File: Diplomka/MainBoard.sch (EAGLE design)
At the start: 2 parts, among them U1 ESP32-WROOM-32

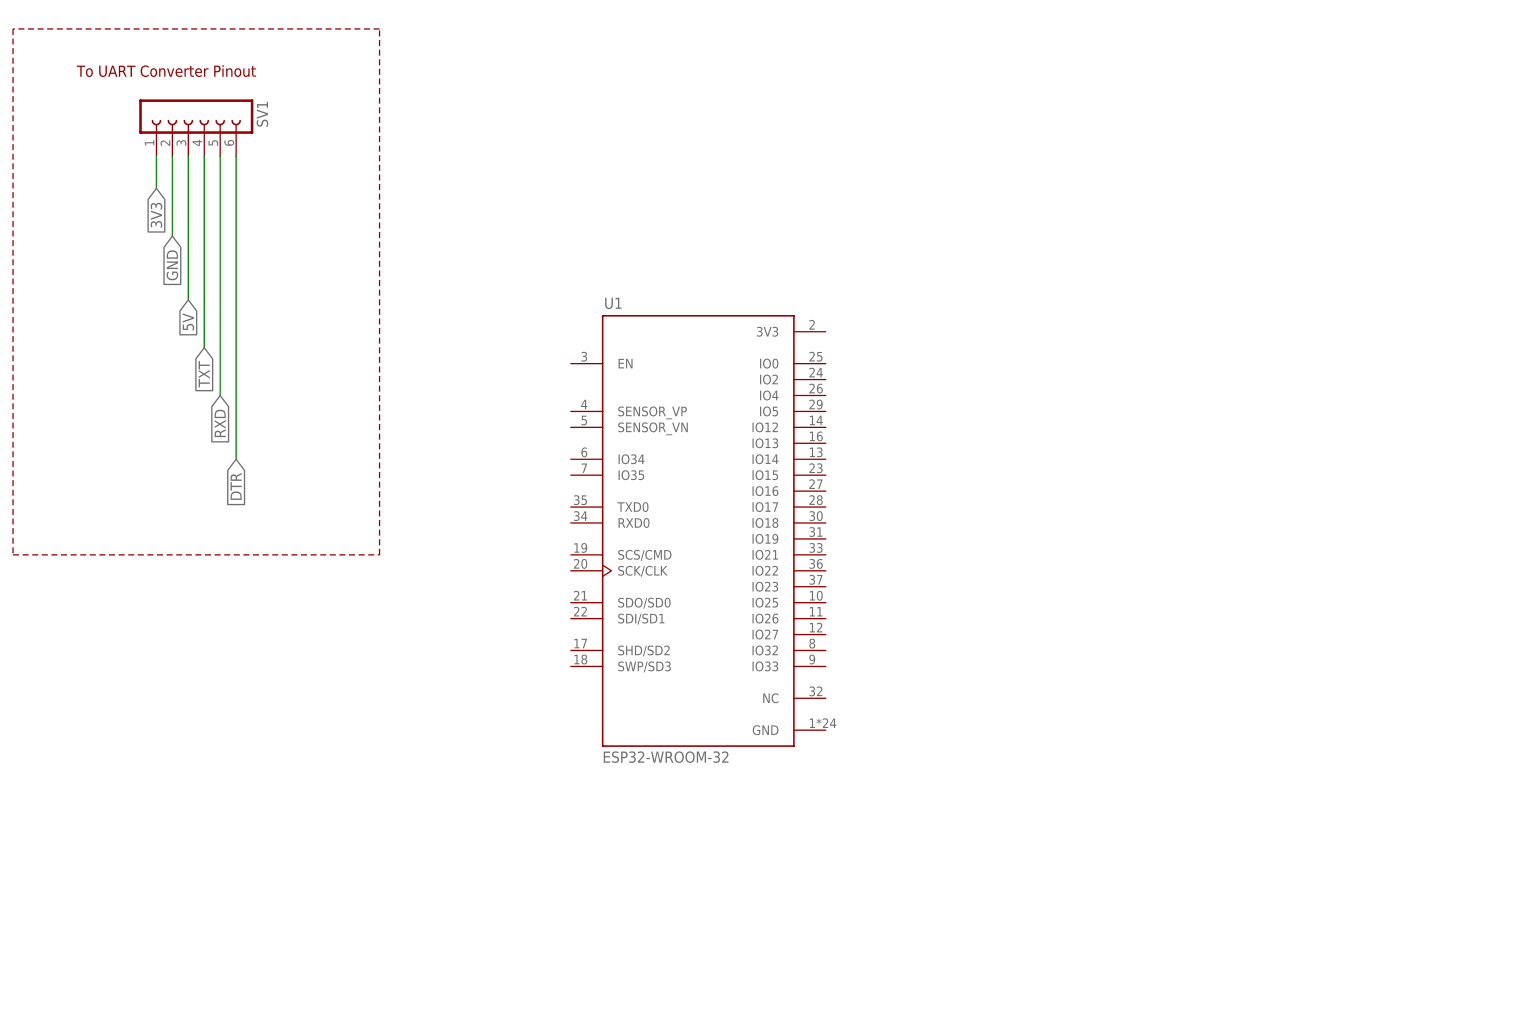
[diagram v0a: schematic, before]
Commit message: Added battery switch IC to schematic and library. 	# Please enter the commit message for your changes. Lines starting 	# with '#' will be ignored, and an empty message aborts the commit. 	# 	# On branch main 	# Your branch is up to date with 'origin/main'. 	# 	# Changes to be committed: 	#	modified:   MainBoard.brd 	#	modified:   MainBoard.s#1 	#	modified:   MainBoard.s#2 	#	modified:   MainBoard.s#3 	#	modified:   MainBoard.s#4 	#	modified:   MainBoard.sch 	#	modified:   eagle.epf 	# 	# Untracked files: 	#	Eagle_WR-USB (rev22c).lbr 	#	MainBoard.b#1 	#	MainBoard.s#5 	#	texas-instruments.lbr 	#
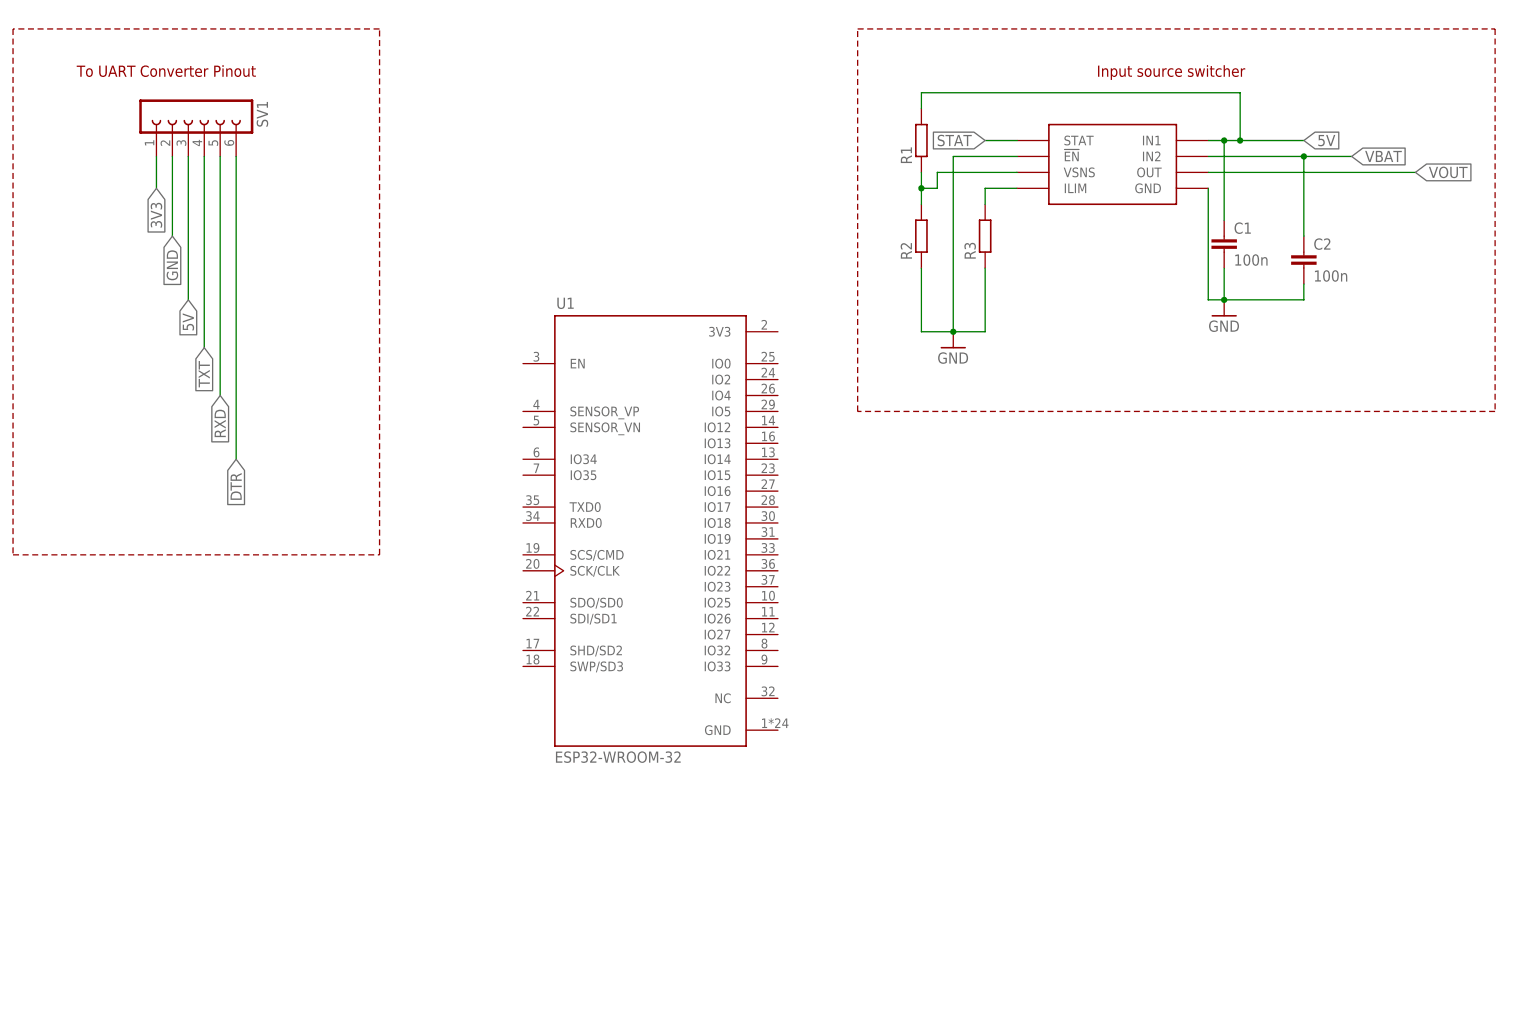
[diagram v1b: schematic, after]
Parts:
- added C1, C2: 100n, rcl:C-EUC0805
- added R1, R2, R3: (no value), rcl:R-EU_R0805
- added U$1: TPS2112A, texas-instruments:TPS2112A
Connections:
- new net N$1: R1.1, R2.2, U$1.VSNS
- new net N$3: R3.2, U$1.ILIM
- new net STAT: U$1.STAT
- new net VBAT: C2.1, U$1.IN2
- new net VOUT: U$1.OUT
- net 5V: now also C1.1, R1.2, U$1.IN1
- net GND: now also C1.2, C2.2, R2.1, R3.1, U$1.!EN, U$1.GND
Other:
- note added: "Input source switcher"
- moved on the sheet: U1

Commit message: Pridan regulator pro 3V3
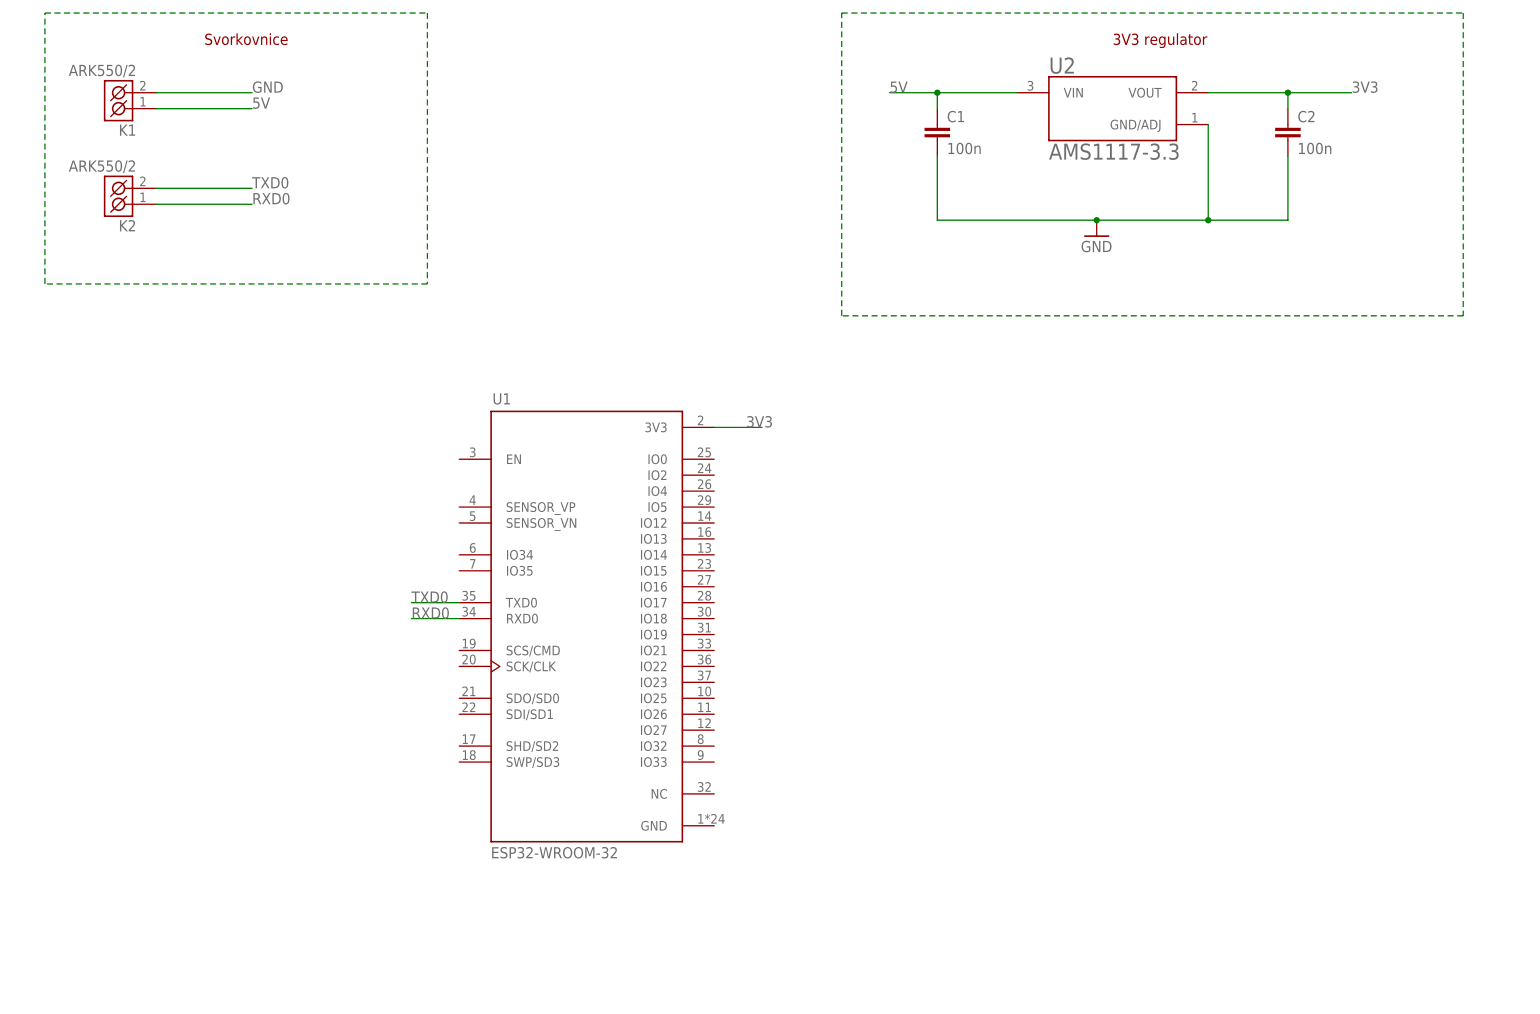
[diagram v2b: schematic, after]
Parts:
- removed R1, R2, R3: (no value), rcl:R-EU_R0805
- removed SV1: (no value), con-lsta:FE06W
- removed U$1: TPS2112A, texas-instruments:TPS2112A
- added K1, K2: ARK550/2, #PaJa_konektory:ARK550/2
- added U2: AMS1117-3.3, AMS1117-3.3:AMS1117-3.3
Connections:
- removed net DTR: SV1.6
- removed net N$1: R1.1, R2.2, U$1.VSNS
- removed net N$3: R3.2, U$1.ILIM
- removed net RXD: SV1.5
- removed net STAT: U$1.STAT
- removed net TXT: SV1.4
- removed net VBAT: C2.1, U$1.IN2
- removed net VOUT: U$1.OUT
- new net RXD0: K2.K1, U1.RXD0
- new net TXD0: K2.K2, U1.TXD0
- net 3V3: now also C2.1, U1.3V3, U2.VOUT; no longer SV1.1
- net 5V: now also K1.K1, U2.VIN; no longer R1.2, SV1.3, U$1.IN1
- net GND: now also K1.K2, U2.GND/ADJ; no longer R2.1, R3.1, SV1.2, U$1.!EN, U$1.GND
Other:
- note added: "3V3 regulator"
- note added: "Svorkovnice"
- note removed: "Input source switcher"
- note removed: "To UART Converter Pinout"
- moved on the sheet: C1, C2, U1

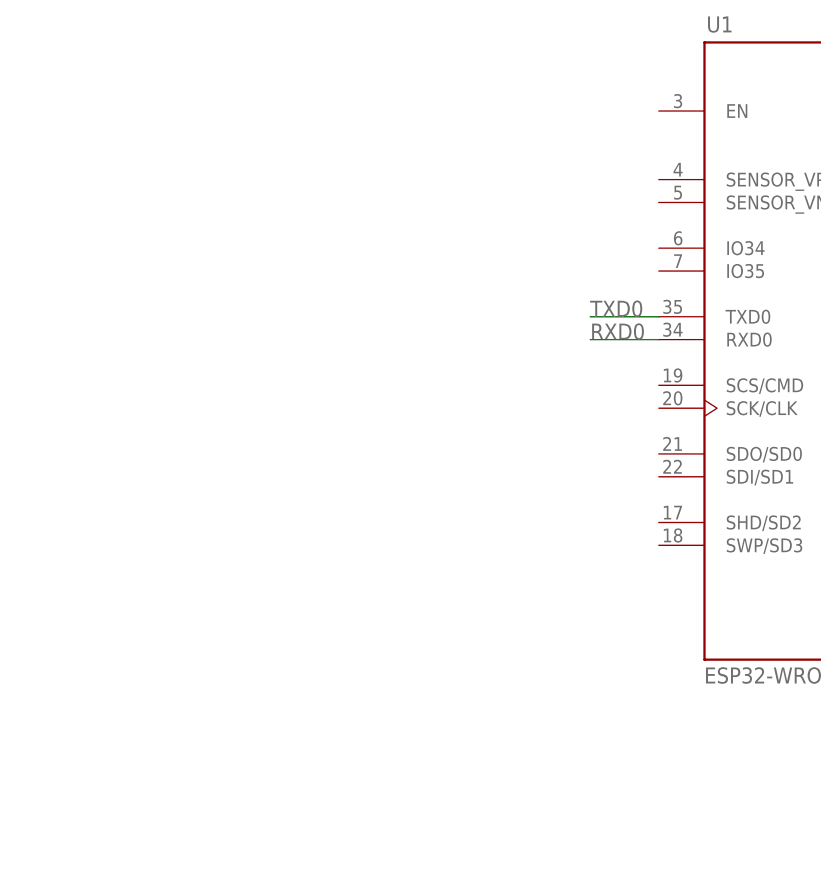
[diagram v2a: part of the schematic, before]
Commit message: Added phototransistor
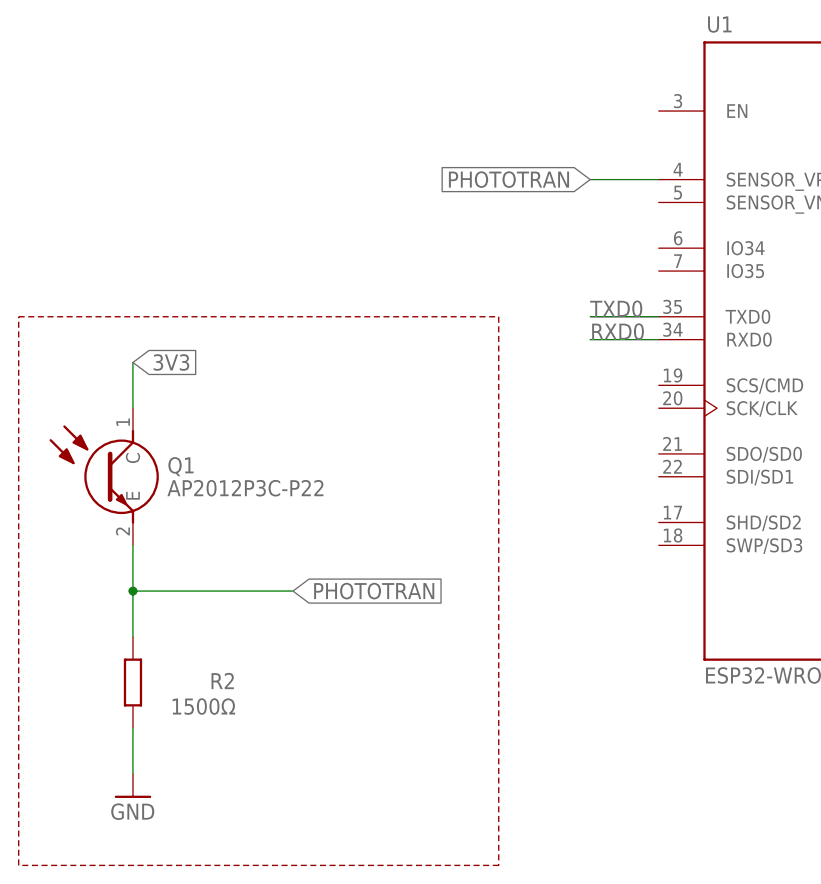
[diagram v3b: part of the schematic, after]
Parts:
- added Q1: AP2012P3C-P22, SamacSys_Parts:AP2012P3C-P22
- added R2: 1500Ω, rcl:R-EU_R0805
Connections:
- new net PHOTOTRAN: Q1.E, R2.2, U1.SENSOR_VP
- net 3V3: now also Q1.C
- net GND: now also R2.1
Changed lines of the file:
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@@
 <part name="C2" library="rcl" library_urn="urn:adsk.eagle:library:334" deviceset="C-EU" device="C0805" package3d_urn="urn:adsk.eagle:package:23617/2" value="100n"/>
 <part name="GND1" library="supply1" library_urn="urn:adsk.eagle:library:371" deviceset="GND" device=""/>
+<part name="R2" library="rcl" library_urn="urn:adsk.eagle:library:334" deviceset="R-EU_" device="R0805" package3d_urn="urn:adsk.eagle:package:23553/2" value="1500Ω"/>
+<part name="Q1" library="SamacSys_Parts" deviceset="AP2012P3C-P22" device=""/>
+<part name="GND2" library="supply1" library_urn="urn:adsk.eagle:library:371" deviceset="GND" device=""/>
 </parts>
 <sheets>
@@
 <text x="40.64" y="165.1" size="1.778" layer="94">Svorkovnice</text>
 <text x="185.42" y="165.1" size="1.778" layer="94">3V3 regulator</text>
+<wire x1="10.16" y1="15.24" x2="10.16" y2="76.2" width="0.1524" layer="94" style="longdash"/>
+<wire x1="10.16" y1="76.2" x2="63.5" y2="76.2" width="0.1524" layer="94" style="longdash"/>
+<wire x1="63.5" y1="76.2" x2="63.5" y2="15.24" width="0.1524" layer="94" style="longdash"/>
+<wire x1="63.5" y1="15.24" x2="10.16" y2="15.24" width="0.1524" layer="94" style="longdash"/>
 </plain>
 <instances>
@@
 <instance part="GND1" gate="1" x="182.88" y="134.62" smashed="yes">
 <attribute name="VALUE" x="180.34" y="132.08" size="1.778" layer="96"/>
+</instance>
+<instance part="R2" gate="G$1" x="22.86" y="35.56" smashed="yes" rot="R90">
+<attribute name="NAME" x="34.29" y="36.6014" size="1.778" layer="95" rot="R180"/>
+<attribute name="VALUE" x="34.29" y="33.782" size="1.778" layer="96" rot="R180"/>
+</instance>
+<instance part="Q1" gate="G$1" x="22.86" y="66.04" smashed="yes">
+<attribute name="NAME" x="26.67" y="59.69" size="1.778" layer="95" align="center-left"/>
+<attribute name="VALUE" x="26.67" y="57.15" size="1.778" layer="96" align="center-left"/>
+</instance>
+<instance part="GND2" gate="1" x="22.86" y="22.86" smashed="yes">
+<attribute name="VALUE" x="20.32" y="20.32" size="1.778" layer="96"/>
 </instance>
 </instances>
@@
 <wire x1="213.36" y1="147.32" x2="213.36" y2="137.16" width="0.1524" layer="91"/>
 </segment>
+<segment>
+<pinref part="GND2" gate="1" pin="GND"/>
+<pinref part="R2" gate="G$1" pin="1"/>
+<wire x1="22.86" y1="25.4" x2="22.86" y2="30.48" width="0.1524" layer="91"/>
+</segment>
 </net>
 <net name="TXD0" class="0">
@@
 <label x="127" y="104.14" size="1.778" layer="95"/>
 </segment>
+<segment>
+<pinref part="Q1" gate="G$1" pin="C"/>
+<wire x1="22.86" y1="66.04" x2="22.86" y2="71.12" width="0.1524" layer="91"/>
+<label x="22.86" y="71.12" size="1.778" layer="95" xref="yes"/>
+</segment>
 </net>
 <net name="N$1" class="0">
@@
 </segment>
 </net>
+<net name="PHOTOTRAN" class="0">
+<segment>
+<wire x1="22.86" y1="45.72" x2="40.64" y2="45.72" width="0.1524" layer="91"/>
+<label x="40.64" y="45.72" size="1.778" layer="95" xref="yes"/>
+<pinref part="R2" gate="G$1" pin="2"/>
+<wire x1="22.86" y1="40.64" x2="22.86" y2="45.72" width="0.1524" layer="91"/>
+<pinref part="Q1" gate="G$1" pin="E"/>
+<wire x1="22.86" y1="45.72" x2="22.86" y2="50.8" width="0.1524" layer="91"/>
+<junction x="22.86" y="45.72"/>
+</segment>
+<segment>
+<pinref part="U1" gate="G$1" pin="SENSOR_VP"/>
+<wire x1="81.28" y1="91.44" x2="73.66" y2="91.44" width="0.1524" layer="91"/>
+<label x="73.66" y="91.44" size="1.778" layer="95" rot="R180" xref="yes"/>
+</segment>
+</net>

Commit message: Some more WIP.
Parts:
- added U$1: HC-SR501, Sensors_PIR_Lux:HC-SR501
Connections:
- new net IO0: U$1.OUT
- net 5V: now also U$1.VCC
- net GND: now also U$1.GND
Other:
- note added: "Koliková lišta pro teplotní/vlhkostní sensor"
- note added: "PIR čidlo"

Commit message: Hotová první verze schématu
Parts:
- added LED1: (no value), led:LEDCHIP-LED0805
- added Q2: BC817-40LT1SMD, transistor-npn:BC817-40LT1SMD
- added R1, R4: 1K, rcl:R-EU_R0805
- added R10, R11, R12: 10k, rcl:R-EU_R0805
- added R3, R5: 2K, rcl:R-EU_R0805
- added R6, R8: 1k, rcl:R-EU_R0805
- added R7: 2k, rcl:R-EU_R0805
- added R9: 150, rcl:R-EU_R0805
- added SW1, SW2, SW3: TACTB-64K-F, #PaJa_prepinace:TACTB-64K-F
- added U$2: MQ2, myParts:MQ2
- added U$3: GY4466, myParts:GY4466
- added U$4: BUZZER, myParts:BUZZER
- added U$5: HTU21D, myParts:HTU21D
- C1, C2: value 100n -> 100uF
- R2: value 1500Ω -> 1.5k
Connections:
- removed net IO0: U$1.OUT
- new net BTN_OUTPUT: R12.1, SW3.1, U1.IO14
- new net BUZZER_CONTROL: R8.1, U1.IO27
- new net I2C_SCL: U$5.SCL, U1.IO22
- new net I2C_SDA: U$5.SDA, U1.IO21
- new net LED_CONTROL: R9.2, U1.IO26
- new net MIC_OUT: U$3.OUT, U1.SENSOR_VN
- new net MQ2_AO: R4.1, R5.2
- new net MQ2_DO: R1.1, R3.2
- new net N$1: Q2.C, U$4.-
- new net N$2: Q2.B, R8.2
- new net N$3: R1.2, U$2.DO
- new net N$4: R4.2, U$2.AO
- new net N$5: LED1.A, R9.1
- new net N$6: R6.2, U$1.OUT
- new net N$7: R10.1, SW1.2, U1.EN
- new net N$8: R11.1, SW2.1, U1.IO0
- new net PIR_DO: R6.1, R7.2, U1.IO2
- net 3V3: now also R10.2, R11.2, R12.2, U$3.VCC, U$5.VIN
- net 5V: now also K1.K2, U$2.VCC, U$4.+; no longer K1.K1
- net GND: now also K1.K1, LED1.C, Q2.E, R3.1, R5.1, R7.1, SW1.1, SW2.2, SW3.2, U$2.GND, U$3.GND, U$5.GND, U1.GND; no longer K1.K2
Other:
- note added: "Bzučák"
- note added: "Fototranzistor - detekce světla"
- note added: "Koliková lišta pro teplotní/ vlhkostní senzor HTU21D"
- note added: "LED indikace"
- note added: "MQ2 Senzor"
- note added: "Mikrofon GY 4466"
- note added: "Uživatelské tlačítko"
- note removed: "Koliková lišta pro teplotní/vlhkostní sensor"
- moved on the sheet: U$1, U1
